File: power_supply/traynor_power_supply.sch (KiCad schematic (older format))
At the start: 34 parts, among them J1 AC IN, J10 OUT2, J11 OUT3, J2 AC IN, J3 Chassis GND, J4 OUT1, J5 TREM, J6 SW, J7 SW, J8 CHOKE, J9 CHOKE

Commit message: Hacking for Feb 1st, 2019
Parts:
- removed C9: 10uF 450V, Capacitor_THT:CP_Radial_D12.5mm_P5.00mm, symbol Device:CP
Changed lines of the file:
@@
 	6350 4850 6350 4450
 Connection ~ 5800 4850
-$Comp
-L Device:CP C9
-U 1 1 5C4CAA84
-P 6850 4300
-F 0 "C9" H 6968 4346 50  0000 L CNN
-F 1 "10uF 450V" H 6968 4255 50  0000 L CNN
-F 2 "Capacitor_THT:CP_Radial_D12.5mm_P5.00mm" H 6888 4150 50  0001 C CNN
-F 3 "~" H 6850 4300 50  0001 C CNN
-	1    6850 4300
-	1    0    0    -1
-$EndComp
 Wire Wire Line
 	6350 3800 6850 3800
-Wire Wire Line
-	6850 3800 6850 4150
 Connection ~ 6350 3800
-Wire Wire Line
-	6350 4850 6850 4850
-Wire Wire Line
-	6850 4850 6850 4450
-Connection ~ 6350 4850
 $Comp
 L Connector:Conn_01x02_Male J11

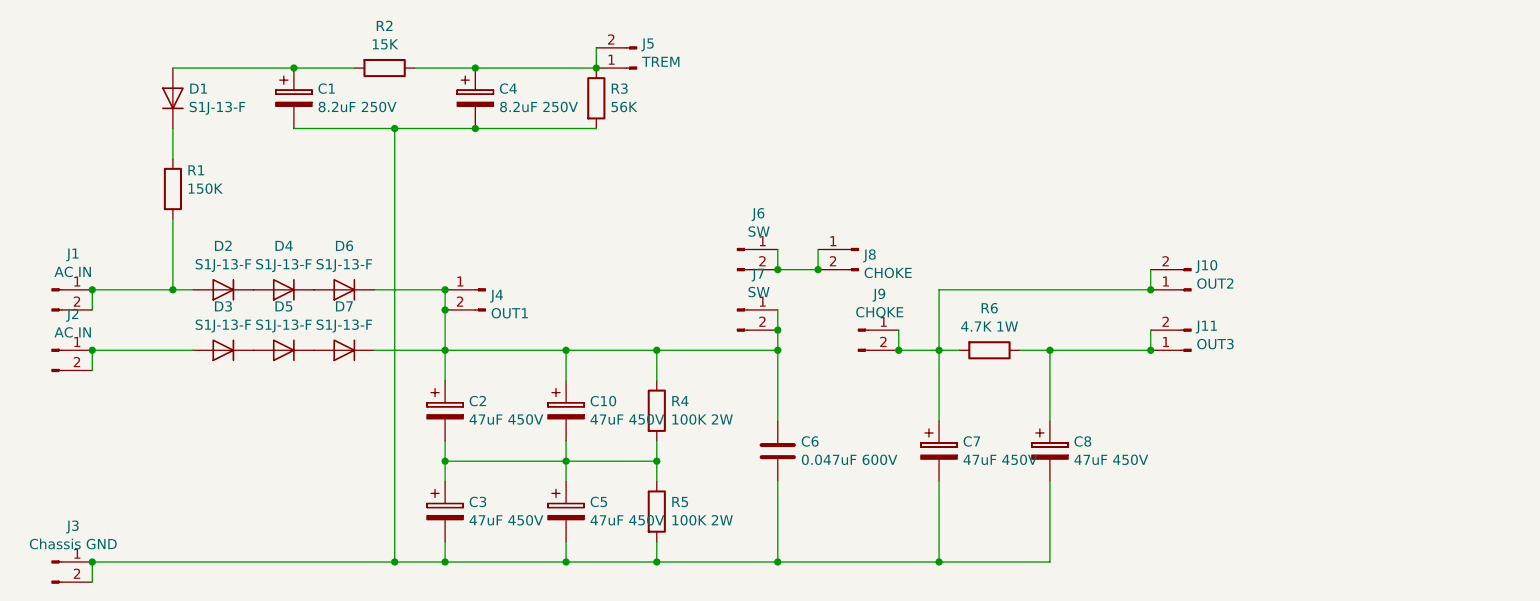
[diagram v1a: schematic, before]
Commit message: Refine schematics
Describe the parts that are mounted on the chassis
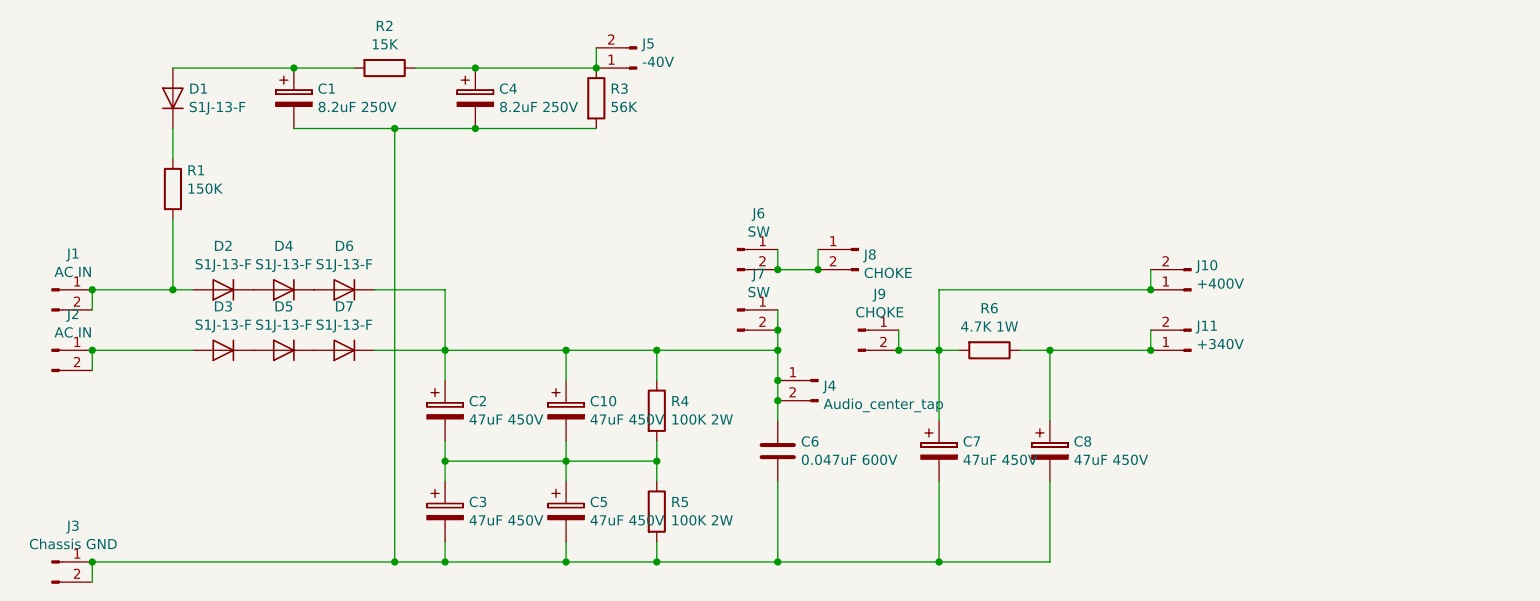
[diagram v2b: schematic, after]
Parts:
- J10: value OUT2 -> +400V
- J11: value OUT3 -> +340V
- J4: value OUT1 -> Audio_center_tap
- J5: value TREM -> -40V
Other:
- moved on the sheet: J4
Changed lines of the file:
@@
 Wire Wire Line
 	3000 3500 3350 3500
-Wire Wire Line
-	3350 3500 3350 3600
 Connection ~ 3350 3800
 Wire Wire Line
@@
 	4400 3800 5000 3800
 Wire Wire Line
-	5000 3800 5000 4150
+	5000 3800 5000 3950
 Connection ~ 4400 3800
 Wire Wire Line
@@
 P 7050 3800
 F 0 "J11" H 7023 3680 50  0000 R CNN
-F 1 "OUT3" H 7023 3771 50  0000 R CNN
+F 1 "+340V" H 7023 3771 50  0000 R CNN
 F 2 "Connector_Wire:SolderWirePad_1x02_P5.08mm_Drill1.5mm" H 7050 3800 50  0001 C CNN
 F 3 "~" H 7050 3800 50  0001 C CNN
@@
 P 7050 3500
 F 0 "J10" H 7023 3380 50  0000 R CNN
-F 1 "OUT2" H 7023 3471 50  0000 R CNN
+F 1 "+400V" H 7023 3471 50  0000 R CNN
 F 2 "Connector_Wire:SolderWirePad_1x02_P5.08mm_Drill1.5mm" H 7050 3500 50  0001 C CNN
 F 3 "~" H 7050 3500 50  0001 C CNN
@@
 P 4300 2400
 F 0 "J5" H 4273 2280 50  0000 R CNN
-F 1 "TREM" H 4273 2371 50  0000 R CNN
+F 1 "-40V" H 4273 2371 50  0000 R CNN
 F 2 "Connector_Wire:SolderWirePad_1x02_P5.08mm_Drill1.5mm" H 4300 2400 50  0001 C CNN
 F 3 "~" H 4300 2400 50  0001 C CNN
@@
 L Connector:Conn_01x02_Male J4
 U 1 1 5C4D8602
-P 3550 3500
-F 0 "J4" H 3523 3473 50  0000 R CNN
-F 1 "OUT1" H 3523 3382 50  0000 R CNN
-F 2 "Connector_Wire:SolderWirePad_1x02_P5.08mm_Drill1.5mm" H 3550 3500 50  0001 C CNN
-F 3 "~" H 3550 3500 50  0001 C CNN
-	1    3550 3500
+P 5200 3950
+F 0 "J4" H 5173 3923 50  0000 R CNN
+F 1 "Audio_center_tap" H 5173 3832 50  0000 R CNN
+F 2 "Connector_Wire:SolderWirePad_1x02_P5.08mm_Drill1.5mm" H 5200 3950 50  0001 C CNN
+F 3 "~" H 5200 3950 50  0001 C CNN
+	1    5200 3950
 	-1   0    0    -1
 $EndComp
-Connection ~ 3350 3500
 Wire Wire Line
 	1600 3600 1600 3500
@@
 	1600 4950 1600 4850
 Connection ~ 1600 4850
-Connection ~ 3350 3600
-Wire Wire Line
-	3350 3600 3350 3800
 Wire Wire Line
 	5000 3300 5000 3400
@@
 Wire Wire Line
 	3950 3800 4400 3800
+Wire Wire Line
+	5000 4050 5000 4150
+Wire Wire Line
+	3350 3500 3350 3800
+Wire Wire Line
+	5000 3950 5000 4050
+Connection ~ 5000 3950
+Connection ~ 5000 4050
 $EndSCHEMATC

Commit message: power supply module
assemble circuit board after it arrived.
update schematic to fix bugs and small improvements we observed while wiring it up.
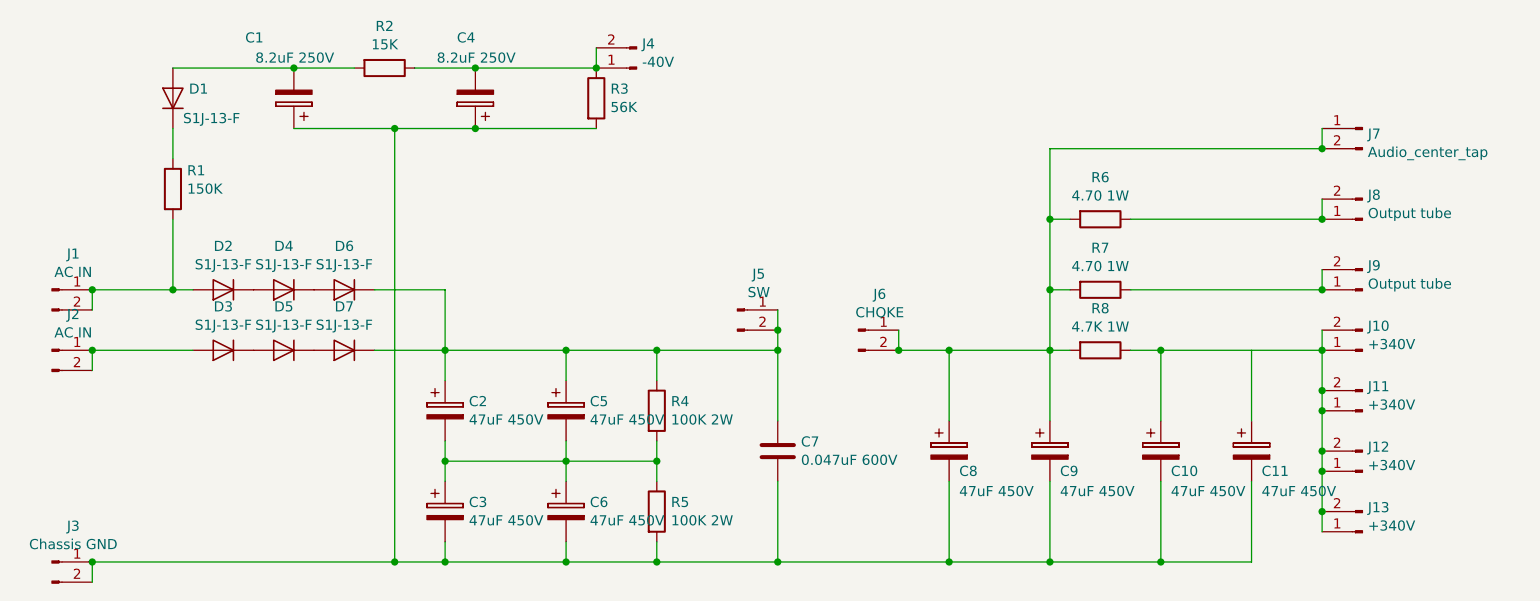
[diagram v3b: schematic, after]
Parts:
- removed J10: +400V, Connector_Wire:SolderWirePad_1x02_P5.08mm_Drill1.5mm, symbol Connector:Conn_01x02_Male
- removed J6: SW, Connector_Wire:SolderWirePad_1x02_P5.08mm_Drill1.5mm, symbol Connector:Conn_01x02_Male
- added C11, C8: 47uF 450V, Capacitor_THT:CP_Radial_D12.5mm_P5.00mm, symbol Device:CP
- added J11, J12, J13: +340V, Connector_Wire:SolderWirePad_1x02_P5.08mm_Drill1.5mm, symbol Connector:Conn_01x02_Male
- added J9: Output tube, Connector_Wire:SolderWirePad_1x02_P5.08mm_Drill1.5mm, symbol Connector:Conn_01x02_Male
- added R6, R7: 4.70 1W, Resistor_THT:R_Axial_DIN0207_L6.3mm_D2.5mm_P10.16mm_Horizontal, symbol Device:R
- J8: value CHOKE -> Output tube
- renumbered C8 to C10, C10 to C5, C5 to C6, C6 to C7, C7 to C9, J11 to J10, J5 to J4, J7 to J5, J9 to J6, J4 to J7, R6 to R8
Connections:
- net at C2.1, C5.1, C7.1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: no longer J7.1 (Pin_1), J7.2 (Pin_2)
- net at C10.2, C3.2, C6.2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: now also C1.1, C4.1, C11.2, C8.2; no longer C1.2, C4.2
- net at J8.1 (Pin_1), J8.2 (Pin_2): now also R6.1
- net at C9.1, J6.1 (Pin_1), J6.2 (Pin_2)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: now also J7.1 (Pin_1), J7.2 (Pin_2), C8.1, R6.2, R7.2
- net at C10.1, J10.1 (Pin_1), J10.2 (Pin_2)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: now also J11.1 (Pin_1), J11.2 (Pin_2), J12.1 (Pin_1), J12.2 (Pin_2), J13.1 (Pin_1), J13.2 (Pin_2)
- net at D1.2 (A), R2.2: now also C1.2; no longer C1.1
- net at J4.1 (Pin_1), J4.2 (Pin_2), R2.1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: now also C4.2; no longer C4.1
- new net: J9.1 (Pin_1), J9.2 (Pin_2), R7.1
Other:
- moved on the sheet: C10, C9, J10, J7, R8
